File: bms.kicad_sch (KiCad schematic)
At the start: 50 parts, among them J9 BAT_PORT, Q16 TPN2R203NC, Q5 AON7544, Q6 AON7544, U7 MAX17320G22+

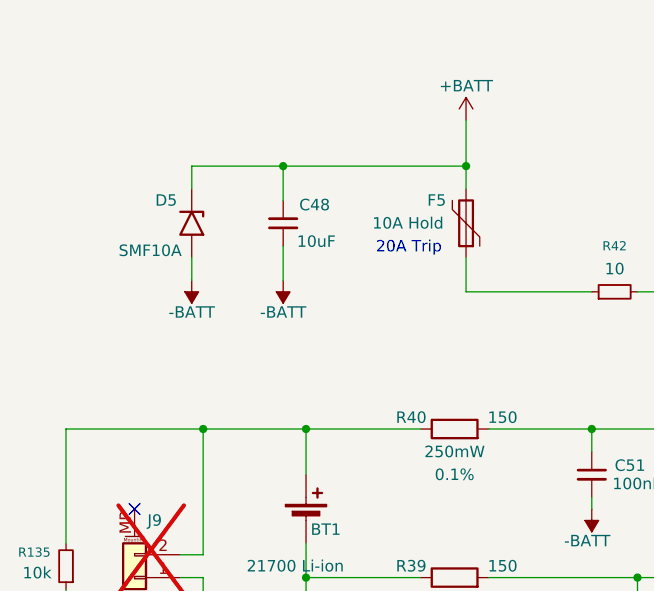
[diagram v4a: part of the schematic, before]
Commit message: Add silkscreen graphics
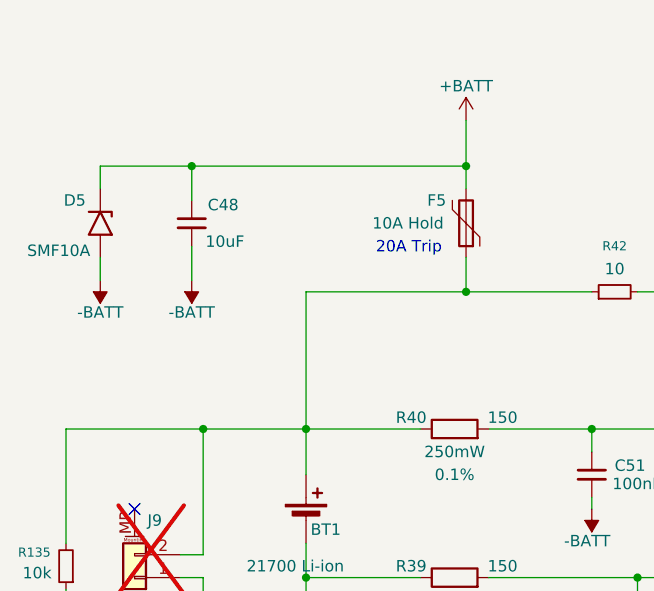
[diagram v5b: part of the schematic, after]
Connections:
- net at BT1.1 (+), J9.2 (Pin_2), R135.2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: now also F5.1, R42.1
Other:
- moved on the sheet: C48, D5
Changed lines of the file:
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@@
 	)
 	(junction
-		(at 67.31 53.34)
+		(at 57.15 53.34)
 		(diameter 0)
 		(color 0 0 0 0)
@@
 	)
 	(junction
+		(at 87.63 67.31)
+		(diameter 0)
+		(color 0 0 0 0)
+	)
+	(junction
 		(at 224.79 55.88)
 		(diameter 0)
@@
 	(wire
 		(pts
-			(xy 67.31 57.15) (xy 67.31 53.34)
+			(xy 57.15 57.15) (xy 57.15 53.34)
 		)
 		(stroke
@@
 	(wire
 		(pts
-			(xy 57.15 53.34) (xy 87.63 53.34)
+			(xy 46.99 53.34) (xy 87.63 53.34)
 		)
 		(stroke
@@
 	(wire
 		(pts
-			(xy 57.15 63.5) (xy 57.15 66.04)
+			(xy 46.99 63.5) (xy 46.99 66.04)
 		)
 		(stroke
@@
 	(wire
 		(pts
+			(xy 87.63 67.31) (xy 69.85 67.31)
+		)
+		(stroke
+			(width 0)
+			(type default)
+		)
+	)
+	(wire
+		(pts
 			(xy 176.53 149.86) (xy 180.34 149.86)
 		)
@@
 	(wire
 		(pts
+			(xy 69.85 67.31) (xy 69.85 82.55)
+		)
+		(stroke
+			(width 0)
+			(type default)
+		)
+	)
+	(wire
+		(pts
 			(xy 200.66 144.78) (xy 176.53 144.78)
 		)
@@
 	(wire
 		(pts
-			(xy 67.31 62.23) (xy 67.31 66.04)
+			(xy 57.15 62.23) (xy 57.15 66.04)
 		)
 		(stroke
@@
 	(wire
 		(pts
-			(xy 57.15 55.88) (xy 57.15 53.34)
+			(xy 46.99 55.88) (xy 46.99 53.34)
 		)
 		(stroke
@@
 	(symbol
 		(lib_id "power:-BATT")
-		(at 67.31 66.04 180)
+		(at 57.15 66.04 180)
 		(unit 1)
 		(body_style 1)
@@
 		(dnp no)
 		(property "Reference" "#PWR0193"
-			(at 67.31 62.23 0)
+			(at 57.15 62.23 0)
 			(hide yes)
 			(show_name no)
@@
 		)
 		(property "Value" "-BATT"
-			(at 67.31 69.596 0)
+			(at 57.15 69.596 0)
 			(show_name no)
 			(do_not_autoplace no)
@@
 		)
 		(property "Footprint" ""
-			(at 67.31 66.04 0)
+			(at 57.15 66.04 0)
 			(hide yes)
 			(show_name no)
@@
 		)
 		(property "Datasheet" ""
-			(at 67.31 66.04 0)
+			(at 57.15 66.04 0)
 			(hide yes)
 			(show_name no)
@@
 		)
 		(property "Description" "Power symbol creates a global label with name \"-BATT\""
-			(at 67.31 66.04 0)
+			(at 57.15 66.04 0)
 			(hide yes)
 			(show_name no)
@@
 	(symbol
 		(lib_id "Diode:SMF10A")
-		(at 57.15 59.69 270)
+		(at 46.99 59.69 270)
 		(unit 1)
 		(body_style 1)
@@
 		(dnp no)
 		(property "Reference" "D5"
-			(at 53.086 57.15 90)
+			(at 42.926 57.15 90)
 			(show_name no)
 			(do_not_autoplace no)
@@
 		)
 		(property "Value" "SMF10A"
-			(at 49.022 62.738 90)
+			(at 38.862 62.738 90)
 			(show_name no)
 			(do_not_autoplace no)
@@
 		)
 		(property "Footprint" "Diode_SMD:D_SOD-123"
-			(at 52.07 59.69 0)
+			(at 41.91 59.69 0)
 			(hide yes)
 			(show_name no)
@@
 		)
 		(property "Datasheet" "https://datasheet.lcsc.com/datasheet/pdf/d549773c39b3657663783a03a169768c.pdf?productCode=C435474"
-			(at 57.15 58.42 0)
+			(at 46.99 58.42 0)
 			(hide yes)
 			(show_name no)
@@
 		)
 		(property "Description" "TVS 10V Vrwm, 17V clamp, 200W 10/1000us, unidirectional, SOD-123"
-			(at 57.15 59.69 0)
+			(at 46.99 59.69 0)
 			(hide yes)
 			(show_name no)
@@
 		)
 		(property "MPN" "SMF10A"
-			(at 52.07 59.69 0)
+			(at 41.91 59.69 0)
 			(hide yes)
 			(show_name no)
@@
 		)
 		(property "Manufacturer" "AnBon"
-			(at 52.07 59.69 0)
+			(at 41.91 59.69 0)
 			(hide yes)
 			(show_name no)
@@
 		)
 		(property "LCSC Part" "C435474"
-			(at 57.15 59.69 0)
+			(at 46.99 59.69 0)
 			(hide yes)
 			(show_name no)
@@
 	(symbol
 		(lib_id "Device:C_Small")
-		(at 67.31 59.69 0)
+		(at 57.15 59.69 0)
 		(unit 1)
 		(body_style 1)
@@
 		(dnp no)
 		(property "Reference" "C48"
-			(at 69.088 57.658 0)
+			(at 58.928 57.658 0)
 			(show_name no)
 			(do_not_autoplace no)
@@
 		)
 		(property "Value" "10uF"
-			(at 68.834 61.722 0)
+			(at 58.674 61.722 0)
 			(show_name no)
 			(do_not_autoplace no)
@@
 		)
 		(property "Footprint" "Capacitor_SMD:C_0805_2012Metric"
-			(at 67.31 59.69 0)
+			(at 57.15 59.69 0)
 			(hide yes)
 			(show_name no)
@@
 		)
 		(property "Datasheet" "https://datasheet.lcsc.com/datasheet/pdf/84e3a6fd29786b629e1e2892084b001d.pdf?productCode=C6119892"
-			(at 67.31 59.69 0)
+			(at 57.15 59.69 0)
 			(hide yes)
 			(show_name no)
@@
 		)
 		(property "Description" "CAP MLCC 10uF ±20% 50V X5R 0805"
-			(at 67.31 59.69 0)
+			(at 57.15 59.69 0)
 			(hide yes)
 			(show_name no)
@@
 		)
 		(property "MPN" "CGA0805X5R106M500MT"
-			(at 67.31 59.69 0)
+			(at 57.15 59.69 0)
 			(hide yes)
 			(show_name no)
@@
 		)
 		(property "Manufacturer" "HRE"
-			(at 67.31 59.69 0)
+			(at 57.15 59.69 0)
 			(hide yes)
 			(show_name no)
@@
 		)
 		(property "LCSC Part" "C6119892"
-			(at 67.31 59.69 0)
+			(at 57.15 59.69 0)
 			(hide yes)
 			(show_name no)
@@
 		)
 		(property "Voltage Rating" "50V"
-			(at 67.31 59.69 0)
+			(at 57.15 59.69 0)
 			(hide yes)
 			(show_name no)
@@
 		)
 		(property "Dielectric" "X5R"
-			(at 67.31 59.69 0)
+			(at 57.15 59.69 0)
 			(hide yes)
 			(show_name no)
@@
 		)
 		(property "Tolerance" "20%"
-			(at 67.31 59.69 0)
+			(at 57.15 59.69 0)
 			(hide yes)
 			(show_name no)
@@
 	(symbol
 		(lib_id "power:-BATT")
-		(at 57.15 66.04 180)
+		(at 46.99 66.04 180)
 		(unit 1)
 		(body_style 1)
@@
 		(dnp no)
 		(property "Reference" "#PWR0194"
-			(at 57.15 62.23 0)
+			(at 46.99 62.23 0)
 			(hide yes)
 			(show_name no)
@@
 		)
 		(property "Value" "-BATT"
-			(at 57.15 69.596 0)
+			(at 46.99 69.596 0)
 			(show_name no)
 			(do_not_autoplace no)
@@
 		)
 		(property "Footprint" ""
-			(at 57.15 66.04 0)
+			(at 46.99 66.04 0)
 			(hide yes)
 			(show_name no)
@@
 		)
 		(property "Datasheet" ""
-			(at 57.15 66.04 0)
+			(at 46.99 66.04 0)
 			(hide yes)
 			(show_name no)
@@
 		)
 		(property "Description" "Power symbol creates a global label with name \"-BATT\""
-			(at 57.15 66.04 0)
+			(at 46.99 66.04 0)
 			(hide yes)
 			(show_name no)
